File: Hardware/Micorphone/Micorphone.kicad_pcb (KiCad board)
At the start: 2 copper layers, 15 x 11.5 mm, 7 parts, among them J1 LAMP1, U1 ICS-40618

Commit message: Update floorplan
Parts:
- J1: moved to F.Cu
- R1, R2: moved to B.Cu
- moved U1 46.0 mm to (105.5, 79.0), turned to -90 degrees
- moved C1 45.8 mm to (101.0, 86.2), turned to -90 degrees
- moved R1 45.6 mm to (101.0, 86.2), turned to 90 degrees
- moved R2 44.2 mm to (103.0, 86.2), turned to -90 degrees
- moved C2 44.0 mm to (103.0, 86.2), turned to -90 degrees
- moved J1 39.4 mm to (107.2, 95.1), turned to 0 degrees
- moved C3 38.0 mm to (109.0, 81.0), turned to -90 degrees
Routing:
- net /MIC_M: track 11.8 -> 0.00 mm, vias 1 -> 0
- net /MIC_P: track 11.5 -> 0.00 mm, vias 1 -> 0
- net GND: track 9.12 -> 0.00 mm, vias 6 -> 2
- net /MIC_BIAS_O: track 7.86 -> 0.00 mm, vias 1 -> 0
- net /MIC-: track 5.94 -> 0.00 mm
- net /MIC+: track 3.75 -> 0.00 mm
- removed copper zone on B.Cu, net GND
- removed copper zone on F.Cu, net GND
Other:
- board size 15 x 11.5 mm -> 14.5 x 28 mm

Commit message: Update Hardware
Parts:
- J1: moved to B.Cu
- moved C3 3.53 mm to (105.9, 82.7), turned to 180 degrees
- moved C1 2.79 mm to (101.5, 83.5)
- moved R1 2.79 mm to (101.5, 83.4)
- moved C2 2.76 mm to (103.2, 83.5)
- moved R2 2.76 mm to (103.2, 83.4)
- moved J1 0.23 mm to (107.5, 95.1), turned to 180 degrees
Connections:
- J1 pad 1: +1V8 -> GND
- J1 pad 2: GND -> /MIC_BIAS_O
- J1 pad 3: /MIC_M -> /MIC_P
- J1 pad 4: /MIC_P -> /MIC_M
- J1 pad 5: /MIC_BIAS_O -> GND
- J1 pad 6: GND -> +1V8
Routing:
- net /MIC_BIAS_O: track 0.00 -> 22.9 mm, vias 0 -> 2
- net /MIC_P: track 0.00 -> 22.6 mm, vias 0 -> 2
- net /MIC_M: track 0.00 -> 19.1 mm, vias 0 -> 2
- net /MIC+: track 0.00 -> 12.6 mm
- net /MIC-: track 0.00 -> 10.6 mm
- net GND: track 0.00 -> 2.57 mm
- added copper zone on B.Cu, net GND
- added copper zone on F.Cu, net GND
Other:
- board size 14.5 x 28 mm -> 14 x 28 mm
- board text added: "1.8v"
- board text added: "GND"
- board text added: "Hackaday"

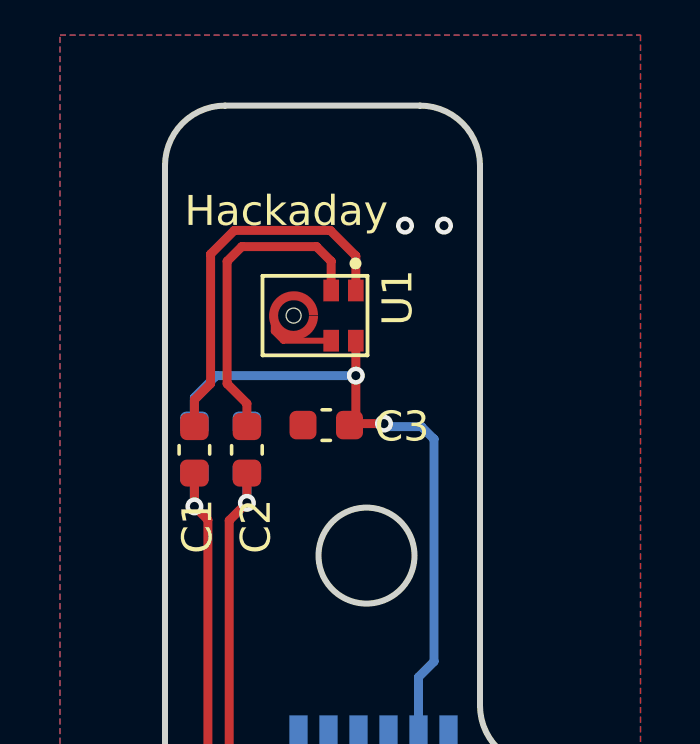
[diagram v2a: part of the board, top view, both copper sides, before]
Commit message: Add labels
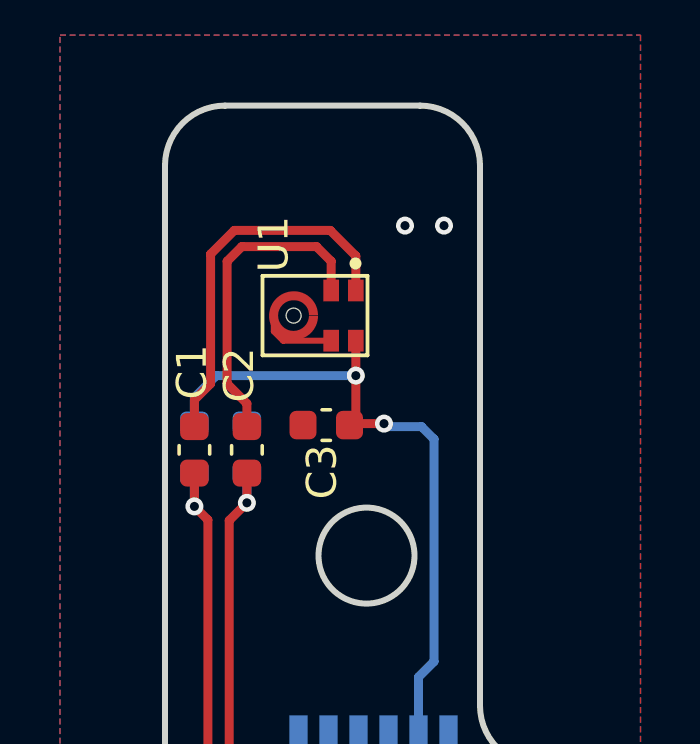
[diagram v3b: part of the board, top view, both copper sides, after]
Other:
- board text added: "Mic"
- board text removed: "1.8v"
- board text removed: "GND"
- board text removed: "Hackaday"
